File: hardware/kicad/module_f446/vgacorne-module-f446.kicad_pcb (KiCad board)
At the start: 2 copper layers, 19.2 x 16.8 mm, 15 parts, among them J1 to main PCB J4, U1 STM32F446RET6, Y1 8MHz

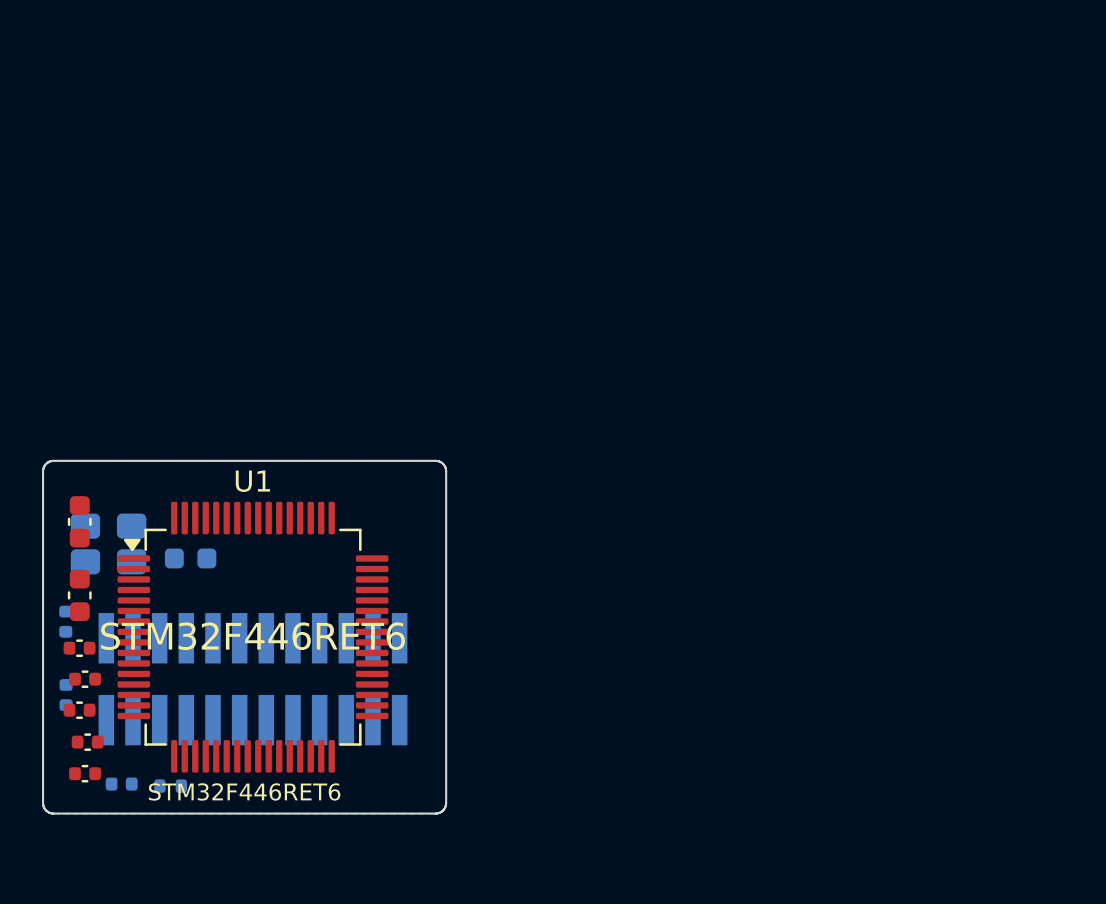
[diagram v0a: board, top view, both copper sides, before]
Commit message: Add trackpad, mouse column and scroll wheel; move MCU and ports
Layout
- MCU module, USB-C and trackpad move to the right half; the left half
  is now the passive satellite.
- VGA daughterboard bay moves to the inner-back corner so both cables
  leave from the back face. The bay sits 4.5 mm further back than the
  keys need, so both halves are 116 mm deep.
- Azoteq TPS65 trackpad, landscape, right beside Y/H/N under a 1 mm
  overlay. The MCU module moves to a PCB ear behind it, next to the
  VGA bay. trackpad.py selects the pad (TPS65 or 40 mm Cirque); the
  case pocket, J5 connector and QMK driver follow the selection.
- Left half: a mouse column beside T/G/B with a scroll wheel (Bourns
  PEC12R) at the top and left/right-click HE keys beside G and B.

Circuits and firmware
- Mux channels reassigned so the satellite's mouse keys and wheel fill
  its three spare channels. The wheel's A/B contacts are summed into
  four voltage levels on one channel.
- QMK: 44-key LAYOUT and a wheel decoder that feeds QMK's quadrature
  encoder driver. Trackpad on I2C1, with rules.mk now generated. The
  host test covers the wheel.
- libhmk: MS_BTN1/MS_BTN2 on the mouse keys (no encoder support).

Case and renders
- Smoother milled case: 7.25 mm walls, 25 mm minimum outside radius
  and a flat back face at the ports.
- render.py builds Blender Cycles renders from the design geometry.

Co-Authored-By: Claude Opus 5.5 (1M context) <noreply@anthropic.com>
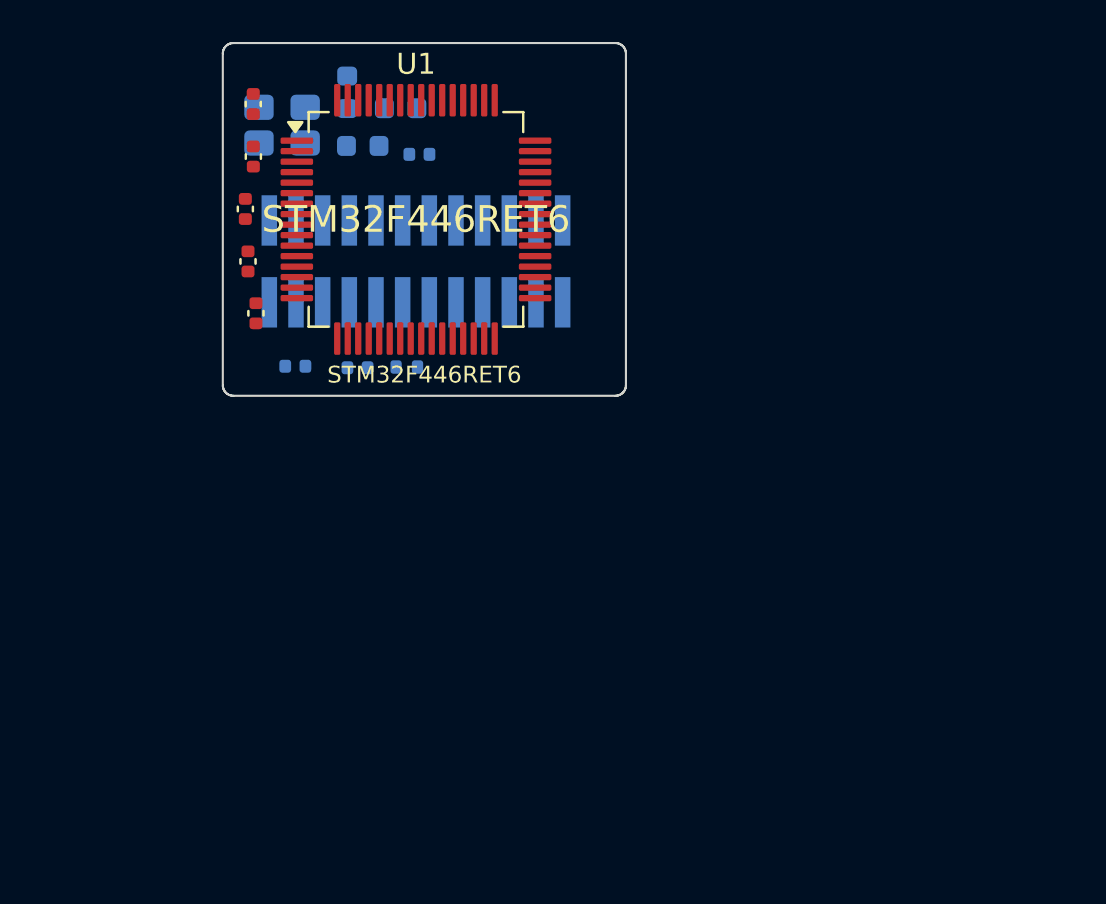
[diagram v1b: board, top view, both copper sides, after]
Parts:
- C5, C7: moved to B.Cu
- moved C11 33.2 mm to (143.9, 29.0)
- moved C6 32.9 mm to (136.0, 26.6), turned to 90 degrees
- moved C4 29.0 mm to (136.0, 29.1), turned to 90 degrees
- moved C5 25.3 mm to (141.2, 28.6), turned to 0 degrees
- moved C7 24.1 mm to (140.5, 26.0)
- moved C8 23.7 mm to (143.0, 26.8)
- moved R1 22.9 mm to (143.3, 39.1)
- moved C3 22.4 mm to (135.6, 31.6), turned to 90 degrees
- moved Y1 21.6 mm to (137.4, 27.6)
- moved C1 21.4 mm to (135.8, 34.1), turned to 90 degrees
- moved J1 21.4 mm to (143.8, 34.1), turned to 90 degrees
- moved U1 21.4 mm to (143.8, 32.1)
- moved C2 20.7 mm to (136.1, 36.6), turned to 90 degrees
- moved C9 19.1 mm to (138.0, 39.1), turned to 0 degrees
- moved C10 18.4 mm to (141.0, 39.2), turned to 0 degrees
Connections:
- J1 pad 1: GND -> /I2C_SCL
- J1 pad 2: GND -> /I2C_SDA
- U1 pad 58: unconnected-(U1-PB6-Pad58) -> /I2C_SCL
- U1 pad 59: unconnected-(U1-PB7-Pad59) -> /I2C_SDA

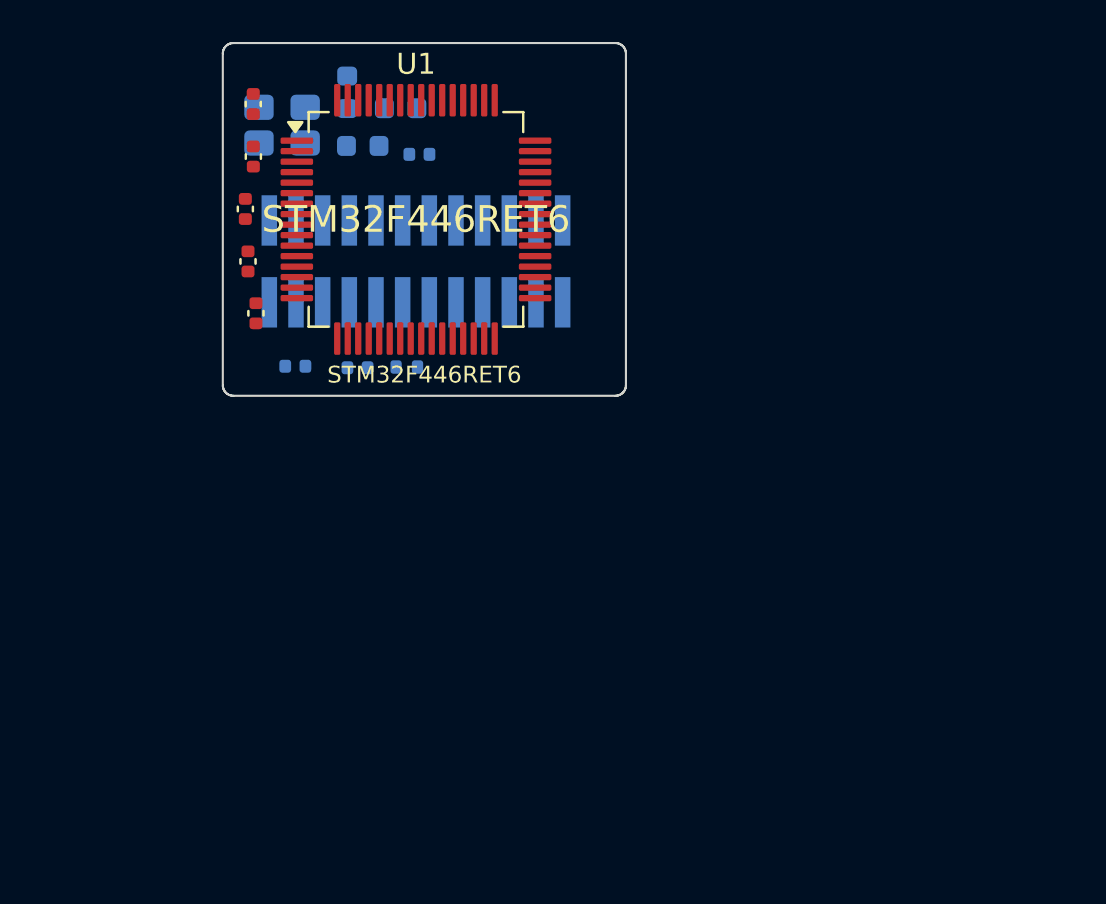
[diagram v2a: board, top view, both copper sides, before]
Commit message: Solder the MCU module flat under the trackpad
The plug-in module stood 8 mm tall on a 2x12 socket, on a PCB ear
behind the trackpad that reached back to the rear face. That kept the
right half's back edge straight across most of the trackpad.

It is now a castellated stamp module:
- 19.4 x 25 mm, with 2x12 half-holes at 1.27 mm and every part on top.
- Soldered onto landing pads J4 on the main PCB's tab, beside Y/H/N,
  under the trackpad.
- About 2.7 mm tall: 1.6 mm below the TPS65's well, 2.2 mm below the
  Cirque's.

With the ear gone, a small PCB tongue under the pad carries its FFC
connector J5. The case back now tapers right from the keys; size and
port positions are unchanged.

- New footprints: castellated module edge and matching landing pads.
- Module boards: all parts on top; a label on the flat underside.
- checks.module_connector now compares castellated hole positions with
  landing pad centres.
- Stack-up: module height and clearance are measured against the
  trackpad well.
- Parts can opt out of the BOM (the module's edge pads are not a part).
- Docs, BOM and images regenerated.

Co-Authored-By: Claude Opus 5.5 (1M context) <noreply@anthropic.com>
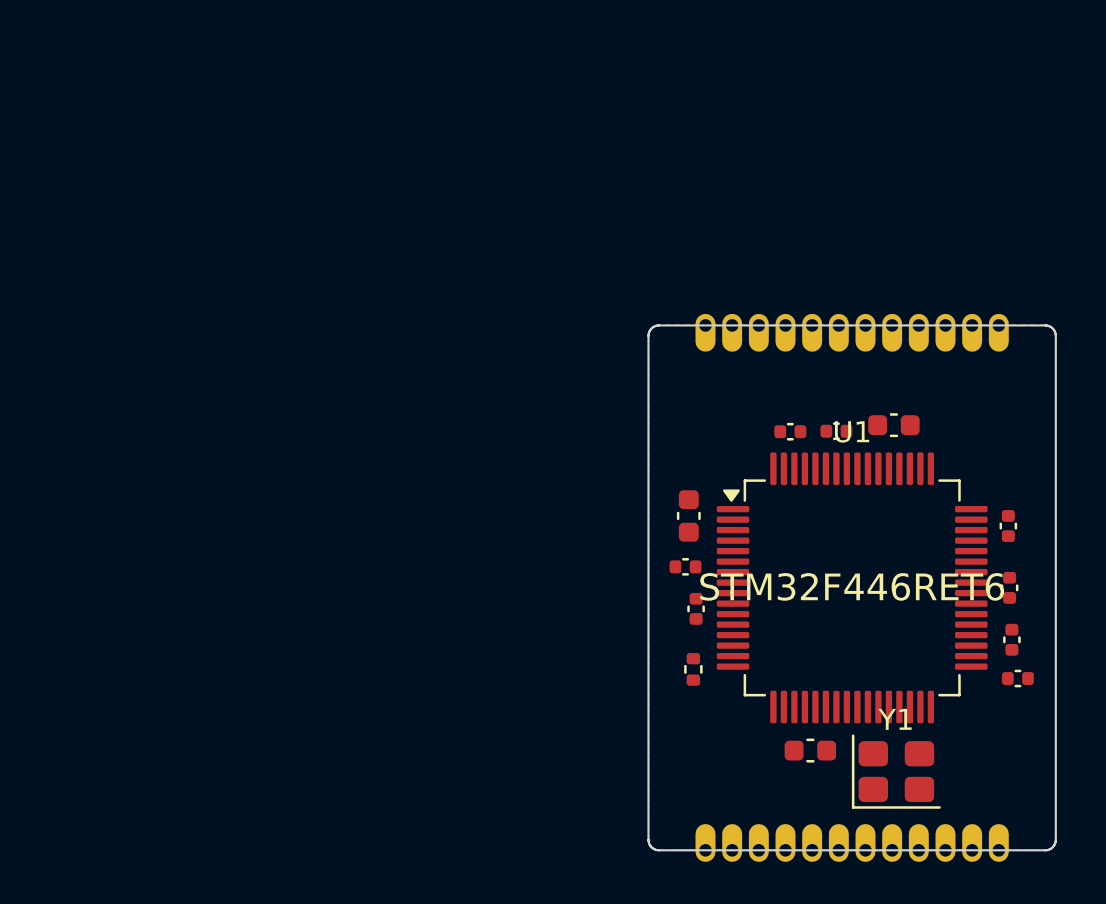
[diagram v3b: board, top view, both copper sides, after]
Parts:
- C10, C11, C5, C7, C8, C9, R1, Y1: moved to F.Cu
- J1: footprint Connector_PinHeader_1.27mm:PinHeader_2x12_P1.27mm_Vertical_SMD -> vgacorne:Module_Castellated_2x12_P1.27mm_19.4x25mm; moved to F.Cu
- moved C4 42.8 mm to (172.1, 52.1)
- moved Y1 42.5 mm to (166.6, 58.4)
- moved C1 39.5 mm to (172.0, 49.6)
- moved C11 37.9 mm to (172.4, 54.0)
- moved C5 35.8 mm to (162.5, 57.4)
- moved C10 31.9 mm to (172.0, 46.7), turned to 90 degrees
- moved C7 30.5 mm to (166.5, 41.9), turned to 0 degrees
- moved C6 30.2 mm to (156.6, 48.6), turned to 0 degrees
- moved C3 30.1 mm to (163.8, 42.2), turned to 0 degrees
- moved U1 27.2 mm to (164.5, 49.6)
- moved J1 26.0 mm to (164.5, 49.6), turned to 0 degrees
- moved C2 25.3 mm to (157.1, 50.6)
- moved C9 23.8 mm to (161.6, 42.2)
- moved C8 23.8 mm to (156.8, 46.2), turned to 90 degrees
- moved R1 19.8 mm to (157.0, 53.5), turned to 90 degrees
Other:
- board size 19.2 x 16.8 mm -> 19.4 x 25 mm

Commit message: Fix design audit findings
Electrical:
- Re-map the castellated module's pads so neighbours on each edge follow
  the LQFP: USB D+/D- together between grounds at the corner nearest the
  USB-C, the six ADC inputs grouped beside +3.3VA, a ground away from the
  select lines.
- Put 1k between each DRV5055 output and its 4.7n cap (TI: no capacitor
  straight on the output).
- STM32F446 module: pull PB2/BOOT1 down so BOOT reaches DFU; pull PA10 up.
- Replace the XC6206 with a second TLV75733, and the link polyfuse with a
  TPS2051C switch (soft start, current limit) so hot-plugging the satellite
  can't brown out the MCU. F1 is now 750 mA.
- USB net class 0.4/0.15 mm: ~97 ohm differential against the pour on both
  2-layer boards (was ~120).
- BOM gains a Tolerance column; part numbers for the F446 crystal.

Mechanical:
- Case foam 2 mm, leaving 0.5 mm under the bottom-side parts (the old stack
  pressed the foam into every sensor).
- USB-C overhangs the ear by 0.46 mm and the opening takes a spec-maximum
  overmould (13.95 x 8.1 mm); the old 11 x 6 mm stopped most plugs short.
- DE-15 rear-mount cutout 20.5 x 11.4 mm; floor pockets under the USB-C and
  encoder pins; plate foam clears the module and the encoder's pins.
- Knob 11.5 mm tall so it clears the encoder's collar.

Docs, PCB images and renders updated to match.

Co-Authored-By: Claude Opus 5.5 (1M context) <noreply@anthropic.com>
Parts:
- added R2: 10k, Resistor_SMD:R_0402_1005Metric, F.Cu at (172.4, 54.0)
- added R3: 10k, Resistor_SMD:R_0402_1005Metric, F.Cu at (160.3, 57.6)
- moved C11 17.5 mm to (159.5, 42.2)
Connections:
- J1 pad 1: /I2C_SCL -> /NRST
- J1 pad 10: GND -> +3.3VA
- J1 pad 11: /ADC_L_A -> +3V3
- J1 pad 12: /ADC_L_B -> /ADC_L_A
- J1 pad 13: /ADC_L_C -> /SWCLK
- J1 pad 14: /ADC_R_A -> /ADC_L_B
- J1 pad 15: /ADC_R_B -> /SWDIO
- J1 pad 16: /ADC_R_C -> /ADC_L_C
- J1 pad 17: /MUX_S0 -> GND
- J1 pad 18: /MUX_S1 -> /ADC_R_A
- J1 pad 19: /MUX_S2 -> /USB_DP
- J1 pad 2: /I2C_SDA -> /MUX_S0
- J1 pad 20: /DET -> /ADC_R_B
- J1 pad 21: /NRST -> /USB_DN
- J1 pad 22: /BOOT -> /ADC_R_C
- J1 pad 23: /SWDIO -> GND
- J1 pad 24: /SWCLK -> /DET
- J1 pad 3: +3V3 -> /BOOT
- J1 pad 4: +3.3VA -> /MUX_S1
- J1 pad 5: +5V -> /I2C_SDA
- J1 pad 6: GND -> /MUX_S2
- J1 pad 7: /USB_DP -> /I2C_SCL
- J1 pad 8: /USB_DN -> GND
- J1 pad 9: GND -> +5V
- U1 pad 28: unconnected-(U1-PB2-Pad28) -> /BOOT1
- U1 pad 43: unconnected-(U1-PA10-Pad43) -> /USART1_RX

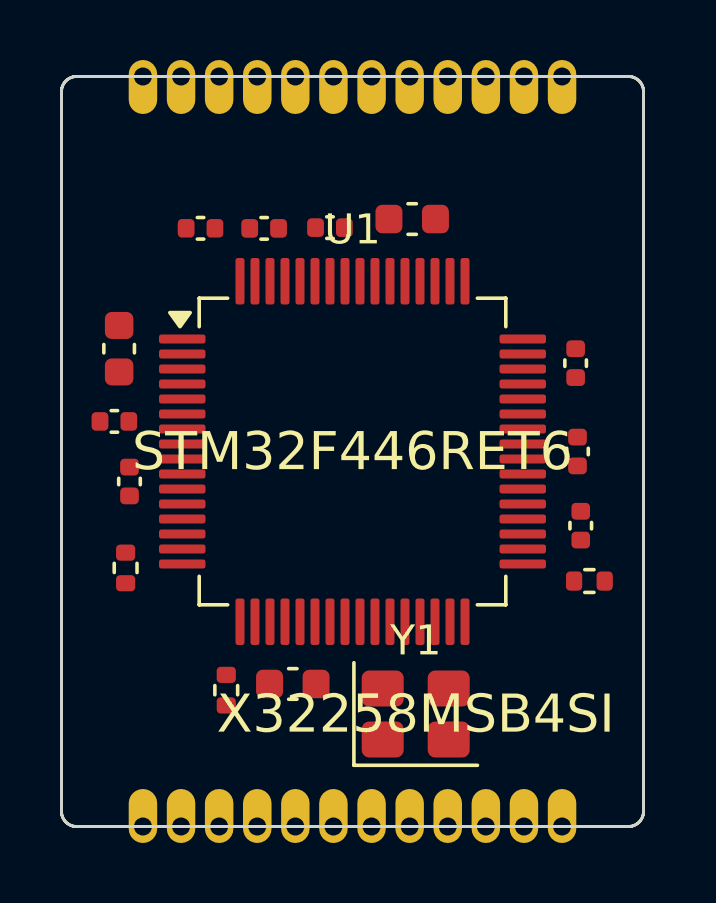
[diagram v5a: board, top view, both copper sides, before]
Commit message: Make the MCU modules 4-layer and route them
The modules are now 1.0 mm 4-layer boards with a solid GND plane on In1
and +3V3 on In2, so every cap and supply pin drops a via and the signals,
USB included, run over unbroken ground. Their support parts are placed
beside the LQFP pins they serve (each 100 nF at its supply pin, the
crystal at the oscillator pins). Module net classes: 0.15 mm clearance,
USB 0.2/0.15 mm (~91 ohm over the plane on JLC's 1.0 mm stack-up).
Castellated pads connect solidly to the planes.

route.py learns to route to castellated edge pads (routing area grown
past the edge, keepouts holding the copper-to-edge clearance), to fan
plane-net pads out to their own vias before routing, and to fall back to
one-pass routing on 2-layer boards. Both modules route completely and
pass DRC.

Also: part-number and tolerance fields no longer print on the
silkscreen.

Co-Authored-By: Claude Opus 5.5 (1M context) <noreply@anthropic.com>
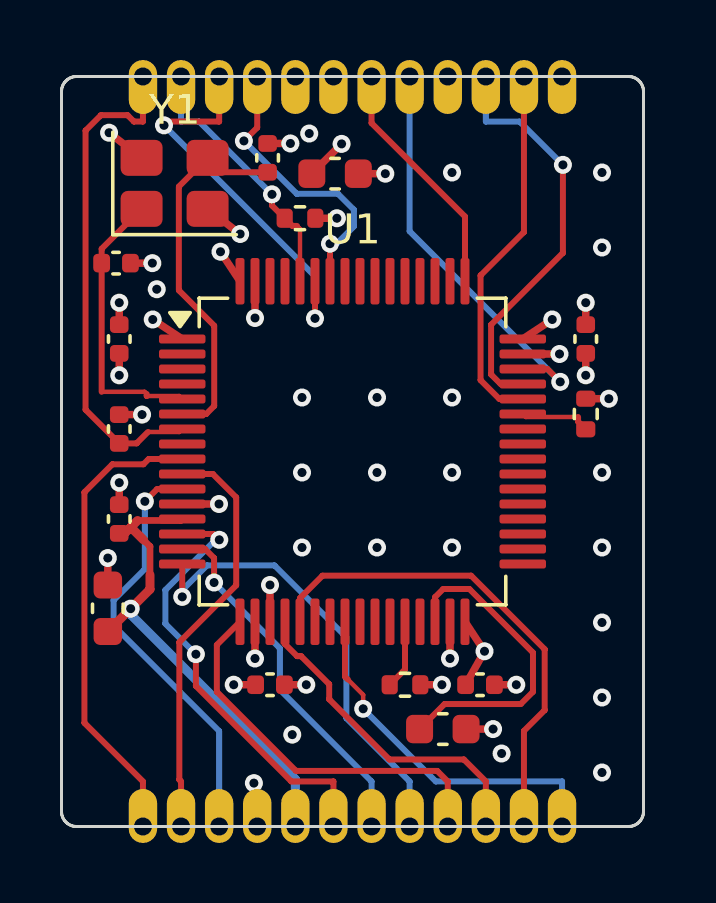
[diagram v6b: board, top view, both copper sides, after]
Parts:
- moved Y1 19.4 mm to (158.6, 40.7)
- moved C5 17.1 mm to (164.0, 40.4)
- moved C8 16.6 mm to (167.5, 58.9), turned to 0 degrees
- moved C7 16.5 mm to (156.4, 54.9), turned to 90 degrees
- moved C3 16.0 mm to (168.8, 57.4)
- moved C1 15.7 mm to (156.8, 45.9)
- moved R3 15.1 mm to (172.3, 48.4)
- moved R1 13.0 mm to (162.8, 41.9), turned to 0 degrees
- moved C10 12.3 mm to (161.7, 39.9)
- moved C2 8.24 mm to (161.8, 57.4), turned to 0 degrees
- moved C11 7.22 mm to (156.8, 48.9), turned to 90 degrees
- moved R2 7.05 mm to (166.3, 57.4)
- moved C4 6.22 mm to (172.3, 45.9)
- moved C9 5.07 mm to (156.7, 43.4)
- moved C6 3.26 mm to (156.8, 51.9), turned to 90 degrees
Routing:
- net GND: track 0.00 -> 18.9 mm, vias 0 -> 42
- net /NRST: track 0.00 -> 16.9 mm
- net /ADC_R_C: track 0.00 -> 16.5 mm
- net +3.3VA: track 0.00 -> 16.2 mm, vias 0 -> 1
- net /MUX_S0: track 0.00 -> 15.7 mm
- net /ADC_L_C: track 0.00 -> 15.3 mm, vias 0 -> 1
- net /ADC_L_A: track 0.00 -> 14.8 mm, vias 0 -> 2
- net /MUX_S2: track 0.00 -> 14.1 mm, vias 0 -> 1
- net /MUX_S1: track 0.00 -> 13.9 mm
- net /USB_DP: track 0.00 -> 13.8 mm, vias 0 -> 1
- net /SWDIO: track 0.00 -> 13.7 mm, vias 0 -> 1
- net /I2C_SDA: track 0.00 -> 13.1 mm, vias 0 -> 2
- net /ADC_R_A: track 0.00 -> 13.1 mm
- net /HSE_OUT: track 0.00 -> 12.5 mm
- net /USB_DN: track 0.00 -> 12.4 mm
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- added copper zone on In2.Cu, net +3V3
- added copper zone on In1.Cu, net GND
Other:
- copper layers 2 -> 4

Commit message: Add JLC fab outputs; switch the HSE crystals to 12 pF load
`generate.py fab` writes each board's JLCPCB files into hardware/fab/
(git-ignored): a Gerber and drill zip with JLC's KiCad settings, and a BOM
and placement file for the parts with an LCSC number. The numbers live in
vgacorne/fab.py, checked against JLC's library on 2026-10-01; the step
lists the parts without one, which are the hand-fitted ones (J4/J5, ENC1,
the daughterboard's socket and pigtail).

The 20 pF-load crystals with 30 pF caps came to gm_crit ~0.96 mA/V
(AN2867), against the STM32F446's 1 mA/V limit, and the caps were outside
the MCUs' 5-25 pF range. Both modules now use YXC's 12 pF versions
(X32258MOB4SI, X322512MOB4SI) with 15 pF caps: ~0.44 mA/V.

Co-Authored-By: Claude Opus 5.5 (1M context) <noreply@anthropic.com>
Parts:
- C10, C9: value 30p -> 15p
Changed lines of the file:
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@@
 			)
 		)
-		(property "Description" "8 MHz, CL 20 pF: matches QMK's generic STM32F446 clock tree; libhmk takes any whole MHz"
+		(property "Description" "8 MHz, CL 12 pF: matches QMK's generic STM32F446 clock tree; libhmk takes any whole MHz"
 			(at 0 0 0)
 			(layer "F.Fab")
@@
 			)
 		)
-		(property "MPN" "X32258MSB4SI"
+		(property "MPN" "X32258MOB4SI"
 			(at 0 0 0)
 			(layer "F.SilkS")
@@
 			)
 		)
-		(property "Value" "30p"
+		(property "Value" "15p"
 			(at 0 1.16 90)
 			(layer "F.Fab")
@@
 			)
 		)
-		(property "Value" "30p"
+		(property "Value" "15p"
 			(at 0 1.16 0)
 			(layer "F.Fab")
